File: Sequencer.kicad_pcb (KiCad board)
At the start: 2 copper layers, 100.6 x 100 mm, 230 parts, among them J1 Conn_02x03_Odd_Even, J2 Conn_02x05_Odd_Even, J3 Conn_02x03_Odd_Even, J4 Conn_01x03, Q1 BC847, Q2 BC847, Q3 BC847, Q4 BC847, SW1 SW_Push, SW10 SW_SPDT_MSM, SW11 SW_SPDT_MSM, SW12 SW_SPDT_MSM, SW2 SW_SPDT_MSM, SW3 SW_SPDT_MSM, SW4 SW_SPDT_MSM, SW5 SW_SPDT_MSM, SW6 SW_SPDT_MSM, SW7 SW_SPDT, SW8 SW_SPDT, SW9 SW_SPDT_MSM, U1 L7805, U10 TL072, U11 74AHCT1G125, U12 TL072, U13 74AHCT1G125, U14 TL072, U2 ATmega328PB-AU, U3 74AHCT1G125, U4 MCP6002-xMS, U5 MCP6002-xMS, U6 MCP6002-xMS, U7 MCP6002-xMS, U8 TL072, U9 74AHCT1G125, X1 20MHz

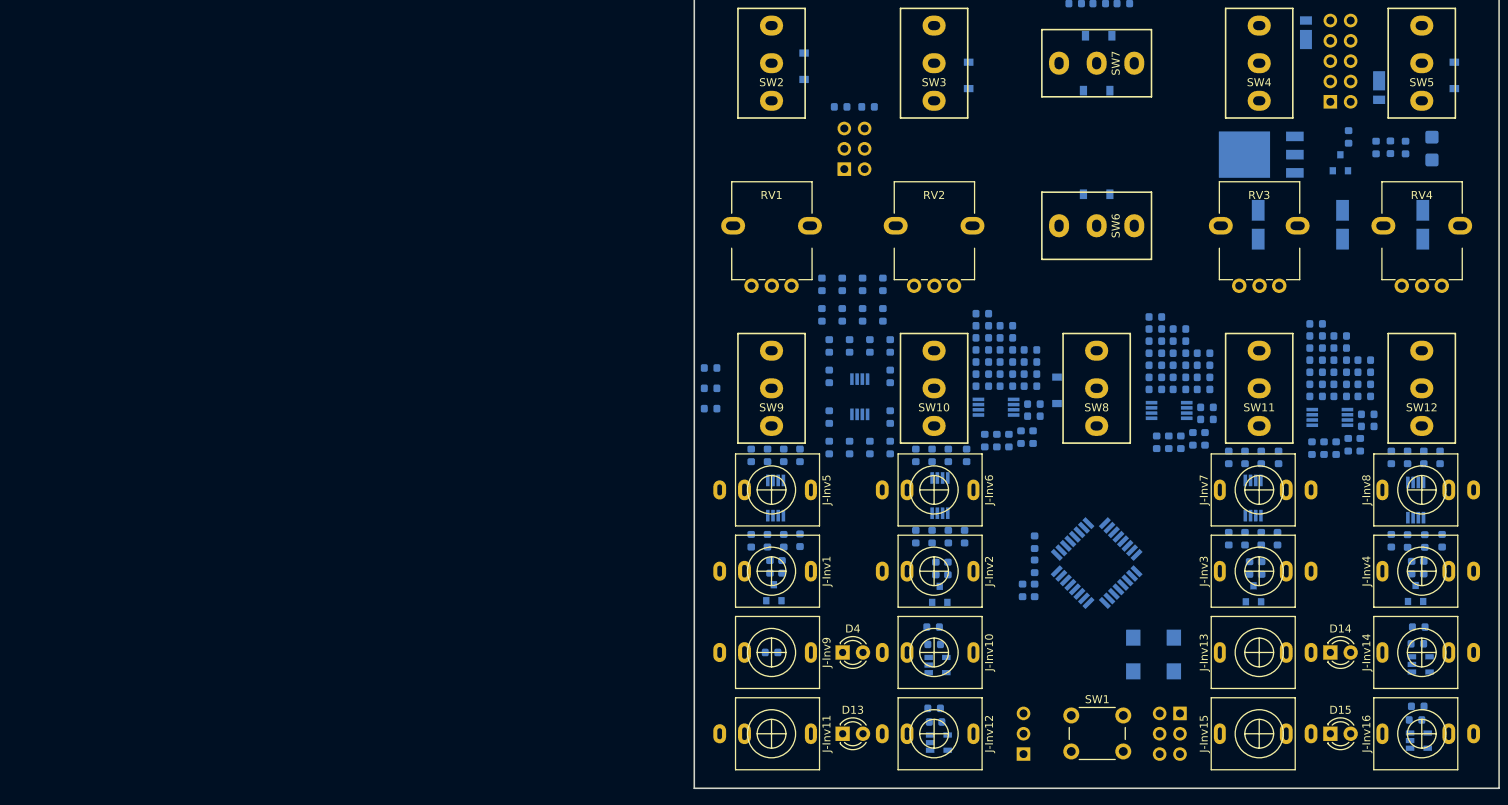
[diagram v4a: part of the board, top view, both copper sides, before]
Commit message: More detailed placement.
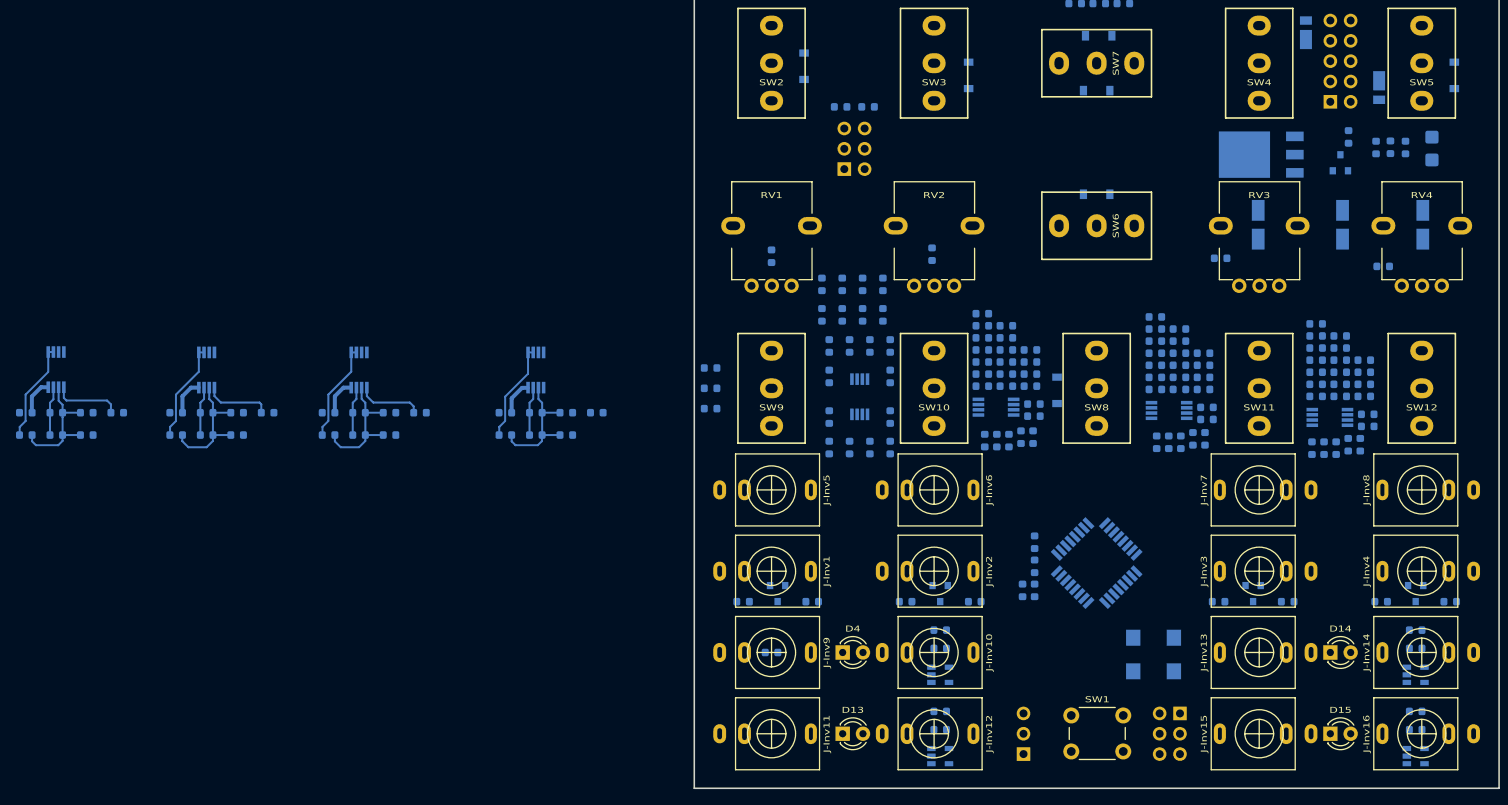
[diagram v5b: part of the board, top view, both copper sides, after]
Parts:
- moved R8 116.0 mm to (14.6, 110.9), turned to 0 degrees
- moved R21 114.6 mm to (52.5, 110.9), turned to 0 degrees
- moved R12 113.9 mm to (18.5, 108.1), turned to 0 degrees
- moved C15 113.6 mm to (52.5, 108.1), turned to 180 degrees
- moved R26 113.6 mm to (74.6, 110.9), turned to 0 degrees
- moved C17 113.5 mm to (56.3, 110.9), turned to 0 degrees
- moved R30 113.2 mm to (78.4, 108.1), turned to 0 degrees
- moved C18 112.9 mm to (74.6, 108.1), turned to 180 degrees
- moved U6 112.9 mm to (56.3, 102.7)
- moved C9 112.3 mm to (14.6, 108.1), turned to 180 degrees
- moved R25 111.9 mm to (56.3, 108.1), turned to 0 degrees
- moved R23 111.8 mm to (60.1, 110.9), turned to 180 degrees
- moved U4 111.6 mm to (18.4, 102.7)
- moved U7 111.2 mm to (78.4, 102.7)
- moved R27 110.6 mm to (82.2, 108.1), turned to 180 degrees
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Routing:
- net +5V: track 0.00 -> 18.0 mm
- net Net-(C14-Pad2): track 0.00 -> 16.6 mm
- net Net-(C17-Pad2): track 0.00 -> 16.6 mm
- net Net-(C11-Pad2): track 0.00 -> 16.4 mm
- net Net-(C20-Pad2): track 0.00 -> 16.3 mm
- net Net-(R8-Pad1): track 0.00 -> 12.5 mm
- net Net-(R16-Pad1): track 0.00 -> 12.5 mm
- net Net-(R21-Pad1): track 0.00 -> 12.5 mm
- net Net-(R26-Pad1): track 0.00 -> 12.5 mm
- net Net-(R11-Pad1): track 0.00 -> 8.60 mm
- net Net-(R19-Pad1): track 0.00 -> 8.39 mm
- net Net-(R24-Pad1): track 0.00 -> 8.24 mm
- net STA0: track 0.00 -> 6.16 mm
- net STA1: track 0.00 -> 6.12 mm
- net END0: track 0.00 -> 6.12 mm
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
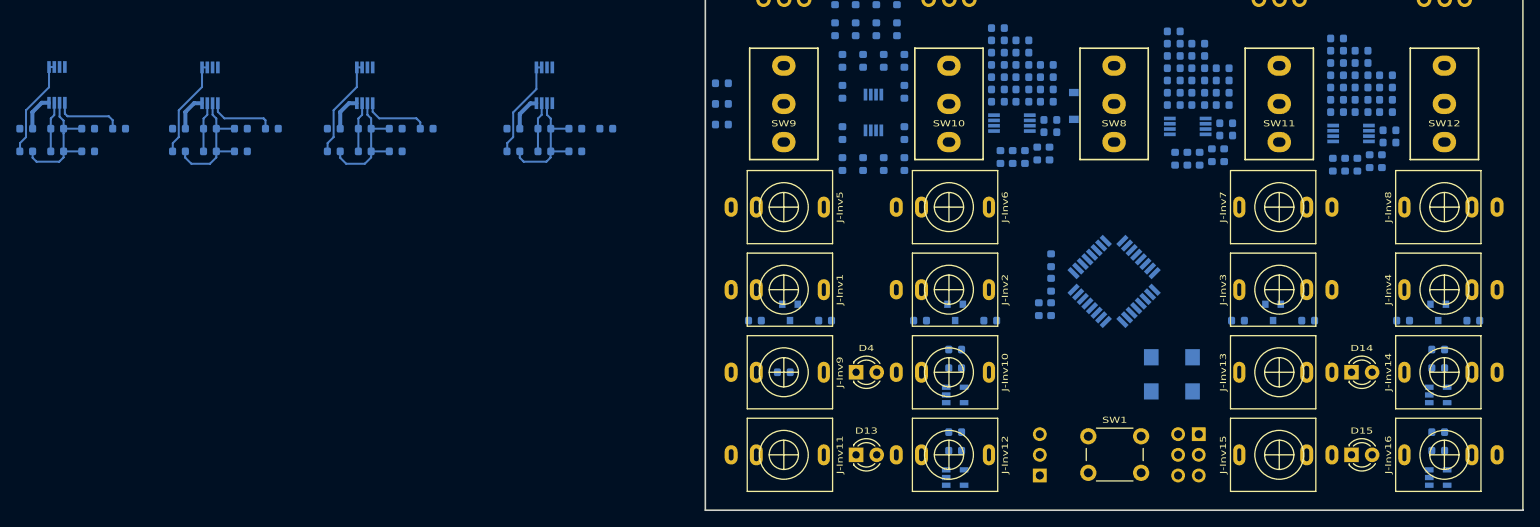
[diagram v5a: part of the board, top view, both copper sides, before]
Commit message: Finished input ADC and digital IO placement.
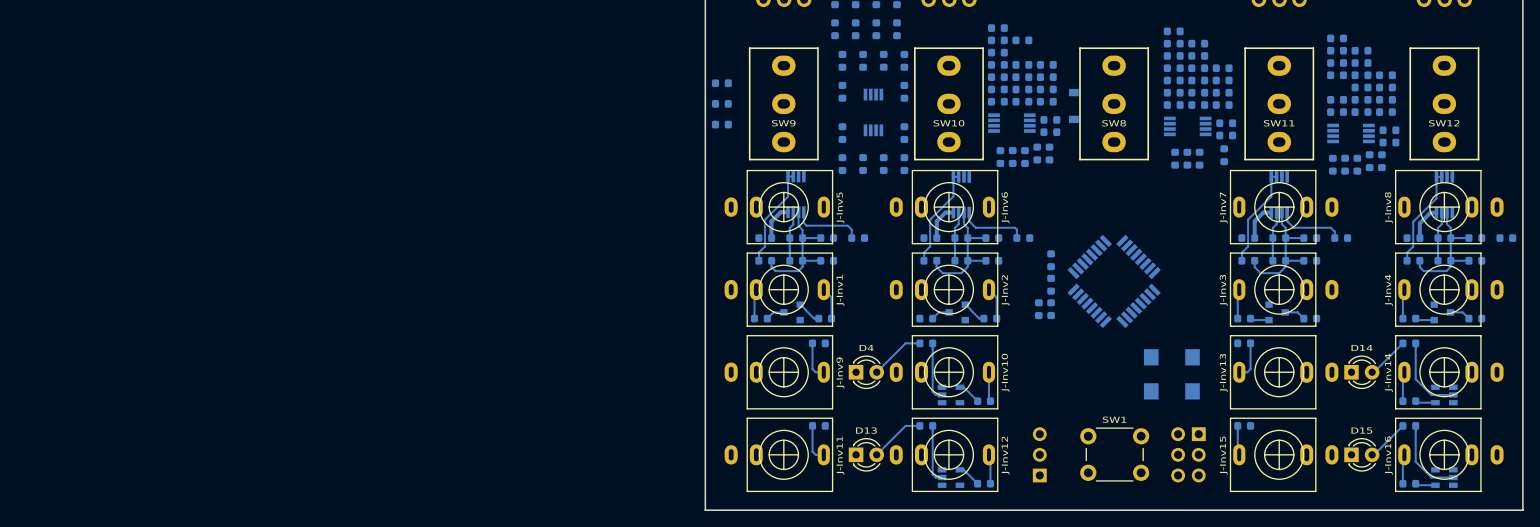
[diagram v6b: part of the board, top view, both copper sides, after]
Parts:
- moved C15 113.3 mm to (165.0, 121.5)
- moved C17 113.3 mm to (168.8, 124.3)
- moved R21 113.3 mm to (165.0, 124.3)
- moved R22 113.3 mm to (172.6, 121.5)
- moved R23 113.3 mm to (172.6, 124.3)
- moved R24 113.3 mm to (176.4, 121.5)
- moved R25 113.3 mm to (168.8, 121.5)
- moved U6 113.3 mm to (168.8, 116.2)
- moved C18 111.6 mm to (185.3, 121.5)
- moved C20 111.6 mm to (189.1, 124.3)
- moved R26 111.6 mm to (185.3, 124.3)
- moved R30 111.6 mm to (189.1, 121.5)
- moved U7 111.6 mm to (189.1, 116.2)
- moved R27 111.6 mm to (192.9, 121.5)
- moved R28 111.6 mm to (192.9, 124.3)
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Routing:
- net TRIG3: track 0.00 -> 9.84 mm
- net TRIG2: track 0.00 -> 9.84 mm
- net TRIG1: track 0.00 -> 7.29 mm
- net TRIG0: track 0.00 -> 7.29 mm
- net Net-(D4-Pad2): track 0.00 -> 6.78 mm
- net Net-(D13-Pad2): track 0.00 -> 6.78 mm
- net Net-(D15-Pad2): track 0.00 -> 5.26 mm
- net Net-(D14-Pad2): track 0.00 -> 5.26 mm
- net /sheet5C25BE7D/Out: track 0.00 -> 4.72 mm
- net /sheet5C230BC3/Out: track 0.00 -> 4.72 mm
- net /CVOut/Out: track 0.00 -> 4.72 mm
- net /sheet5C188821/In: track 0.00 -> 3.95 mm
- net /DigitalIn/In: track 0.00 -> 3.95 mm
- net +5V: track 18.0 -> 21.6 mm
- net /sheet5C25BEB7/Out: track 0.00 -> 3.63 mm
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
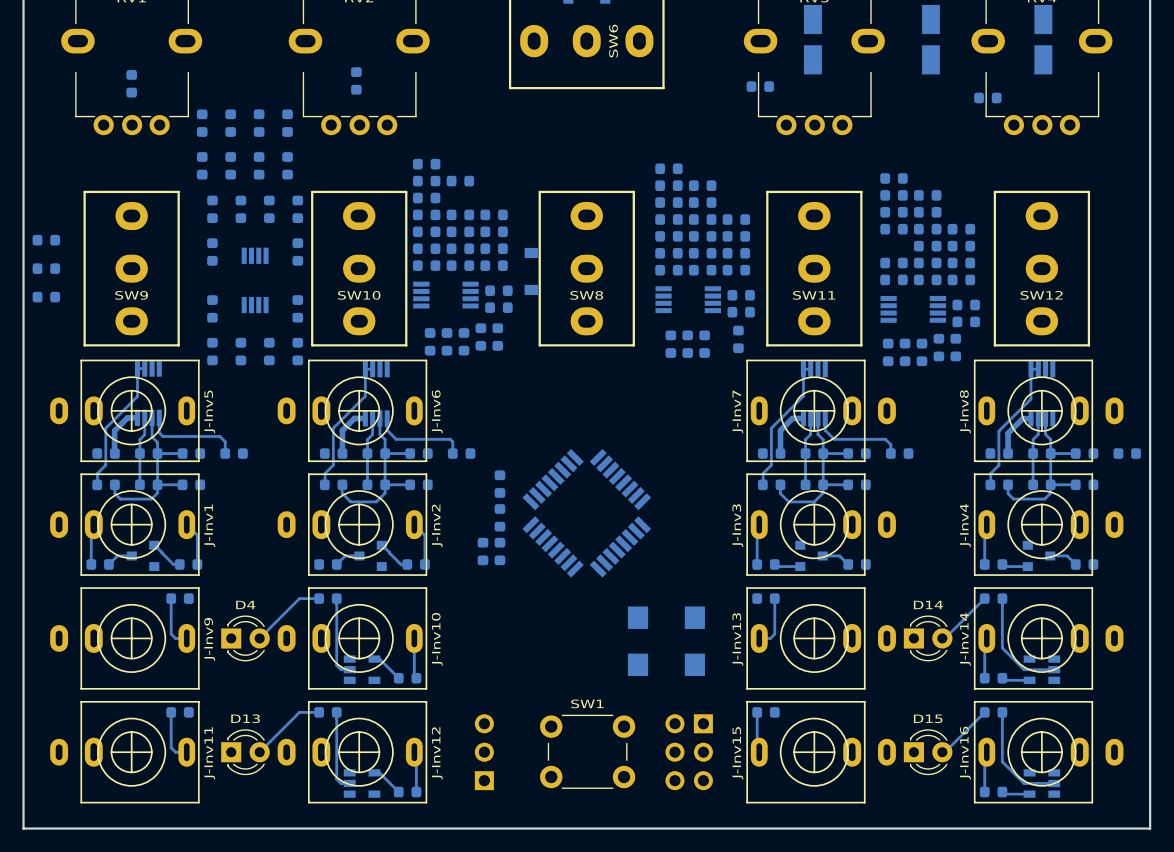
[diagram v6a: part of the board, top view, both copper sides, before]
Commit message: PWM filter placement.
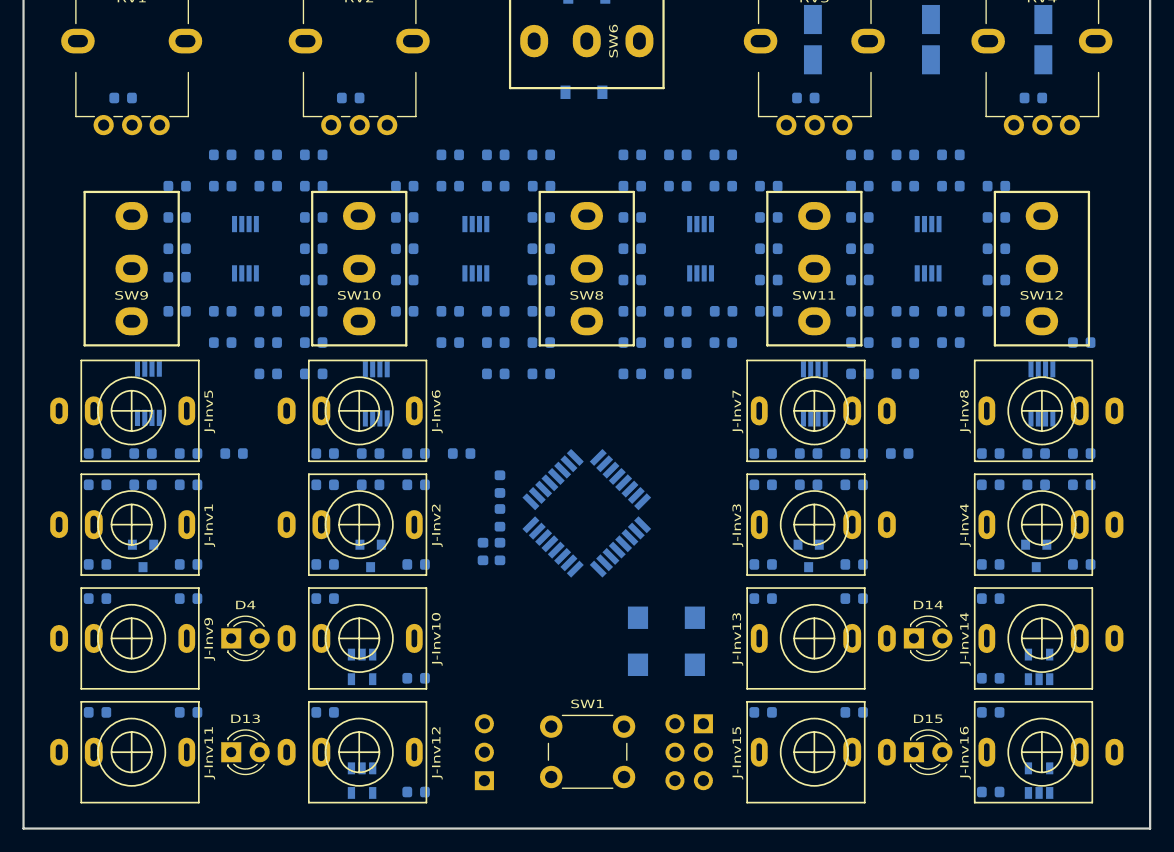
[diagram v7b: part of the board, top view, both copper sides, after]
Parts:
- moved R71 57.1 mm to (104.8, 144.6), turned to 180 degrees
- moved R107 41.3 mm to (172.4, 144.6)
- moved R53 36.2 mm to (104.8, 134.5), turned to 180 degrees
- moved R89 35.1 mm to (172.4, 134.5)
- moved C23 22.5 mm to (124.1, 114.4), turned to 180 degrees
- moved R39 22.4 mm to (120.1, 114.4), turned to 180 degrees
- moved R44 17.7 mm to (120.1, 94.8), turned to 180 degrees
- moved C51 17.7 mm to (176.9, 94.8), turned to 0 degrees
- moved D12 16.7 mm to (148.2, 89.3), turned to 0 degrees
- moved R40 16.5 mm to (124.1, 111.6), turned to 180 degrees
- moved R48 16.1 mm to (111.9, 100.4), turned to 180 degrees
- moved R82 15.9 mm to (164.8, 97.6), turned to 0 degrees
- moved C22 15.6 mm to (120.1, 97.6), turned to 0 degrees
- moved R105 15.5 mm to (181.0, 111.6), turned to 180 degrees
- moved R45 15.3 mm to (116.0, 97.6), turned to 0 degrees
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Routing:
- net +5V: track 21.6 -> 0.00 mm
- net Net-(C14-Pad2): track 16.6 -> 0.00 mm
- net Net-(C17-Pad2): track 16.6 -> 0.00 mm
- net Net-(C11-Pad2): track 16.4 -> 0.00 mm
- net Net-(C20-Pad2): track 16.3 -> 0.00 mm
- net Net-(R8-Pad1): track 12.5 -> 0.00 mm
- net Net-(R26-Pad1): track 12.5 -> 0.00 mm
- net Net-(R21-Pad1): track 12.5 -> 0.00 mm
- net Net-(R16-Pad1): track 12.5 -> 0.00 mm
- net TRIG3: track 9.84 -> 0.00 mm
- net TRIG2: track 9.84 -> 0.00 mm
- net Net-(R11-Pad1): track 8.60 -> 0.00 mm
- net Net-(R19-Pad1): track 8.39 -> 0.00 mm
- net Net-(R24-Pad1): track 8.24 -> 0.00 mm
- net TRIG1: track 7.29 -> 0.00 mm
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
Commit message: Minor placement adjustments.
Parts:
- moved R74 10.8 mm to (192.7, 134.5)
- moved R92 10.8 mm to (192.7, 144.6)
- moved R56 7.11 mm to (133.3, 144.6)
- moved R6 7.11 mm to (133.3, 134.5)
- moved Q3 2.84 mm to (167.8, 127.9), turned to 0 degrees
- moved Q4 2.84 mm to (188.1, 127.9), turned to 0 degrees
- moved Q1 2.79 mm to (108.9, 127.9), turned to 180 degrees
- moved Q2 2.79 mm to (129.2, 127.9), turned to 180 degrees
- moved U3 2.59 mm to (128.9, 138.0), turned to 0 degrees
- moved U9 2.59 mm to (128.9, 148.2), turned to 0 degrees
- moved U11 2.59 mm to (188.4, 138.0), turned to 180 degrees
- moved U13 2.59 mm to (188.4, 148.2), turned to 180 degrees
- moved U5 0.76 mm to (128.9, 116.2)
- moved U4 0.73 mm to (108.6, 116.2)
- moved U7 0.51 mm to (188.6, 116.2)
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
